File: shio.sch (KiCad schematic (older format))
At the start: 82 parts, among them J1 10118193-0001LF, U1 LM66100DCKT, U2 MAX38640AENT+, U3 NRF52840-CKAA-R7, U4 LM66100DCKT, U5 BMA400, U6 W25N01GVZEIG_TR, U8 SiP32431DR3, Y1 32.768kHz, Y3 32MHz

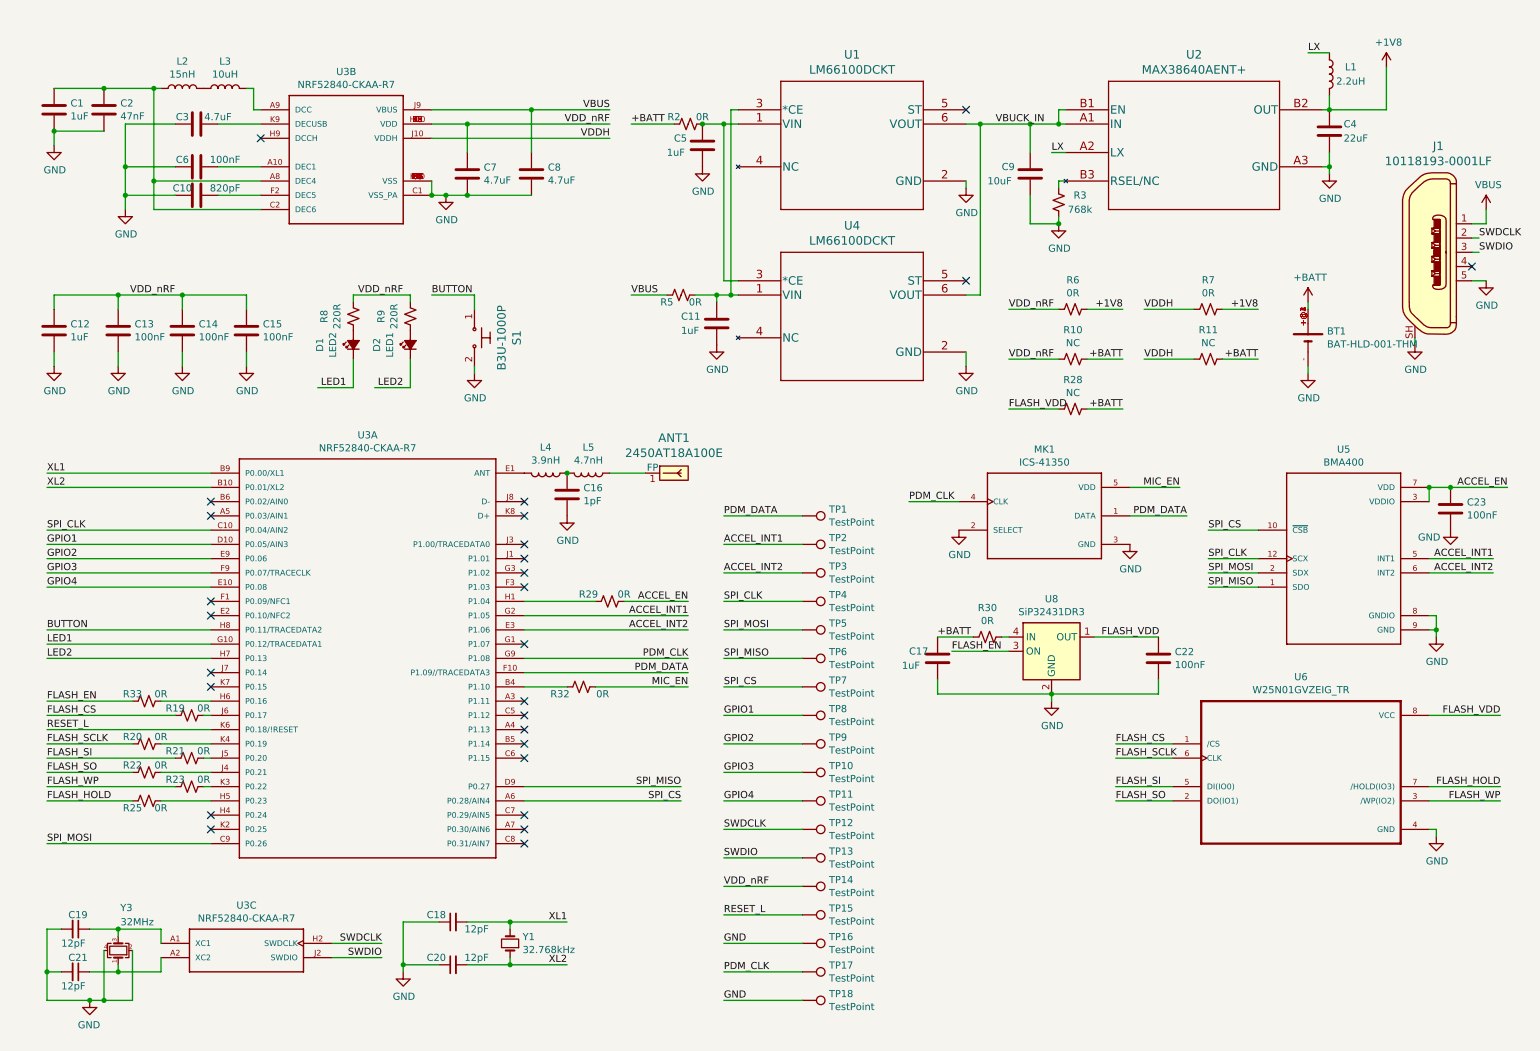
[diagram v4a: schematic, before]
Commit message: Cleaned up schematic, modified sheet
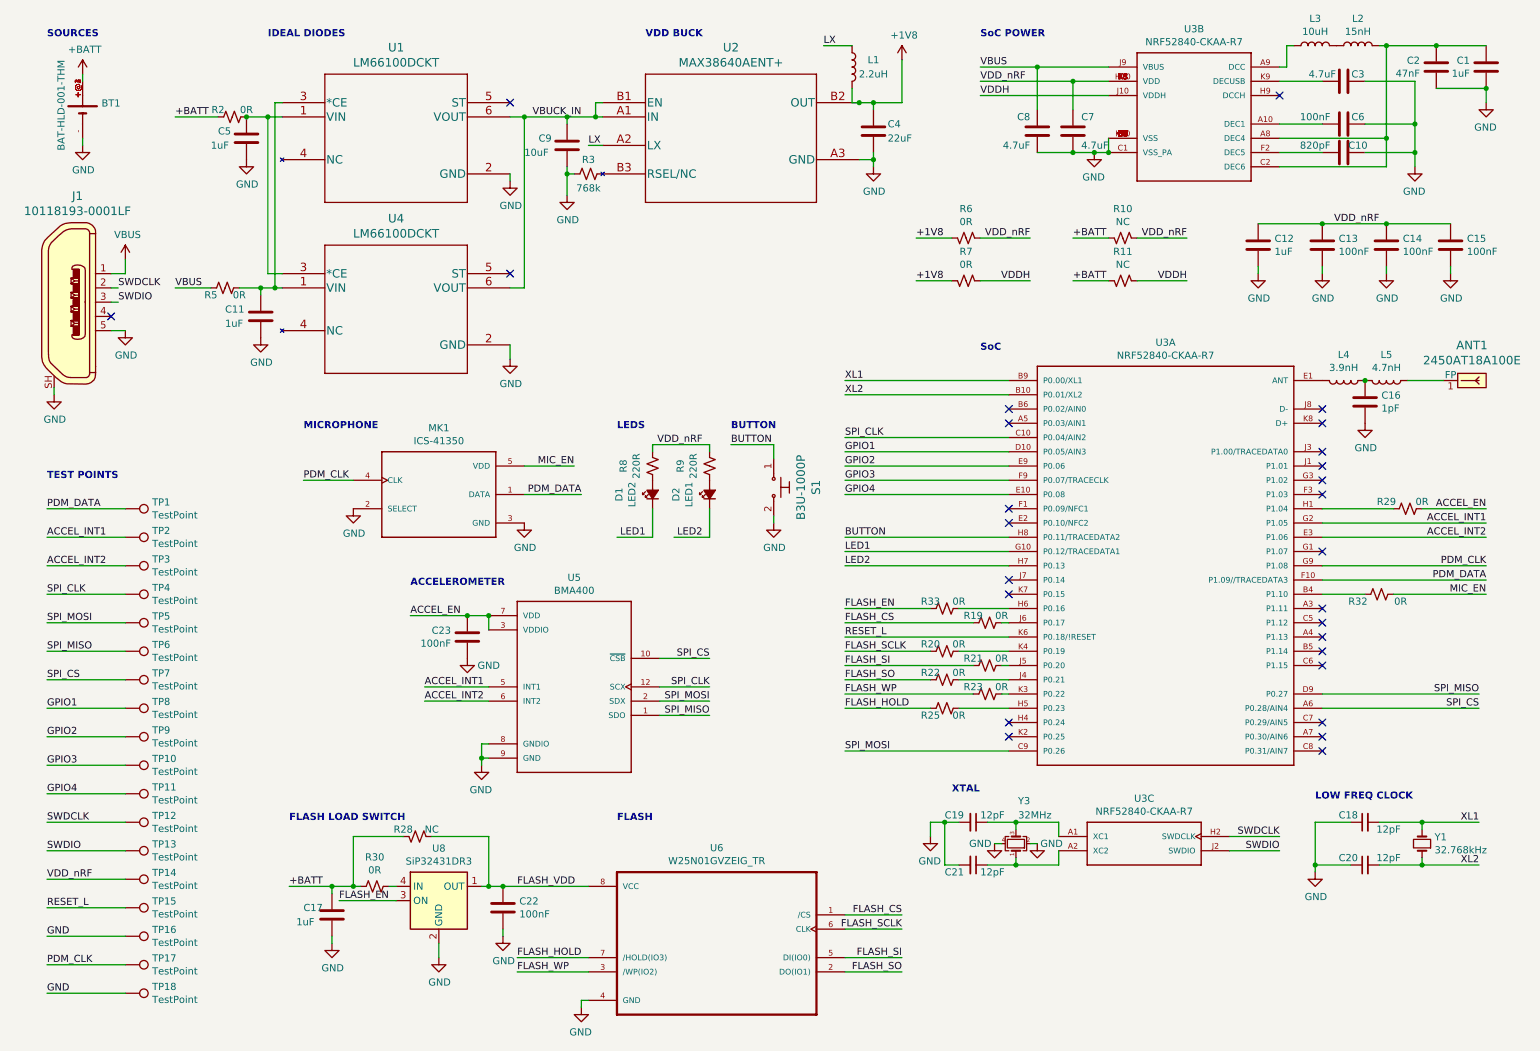
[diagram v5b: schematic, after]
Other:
- note added: "ACCELEROMETER"
- note added: "BUTTON"
- note added: "FLASH"
- note added: "FLASH LOAD SWITCH"
- note added: "IDEAL DIODES"
- note added: "LEDS"
- note added: "LOW FREQ CLOCK"
- note added: "MICROPHONE"
- note added: "SOURCES"
- note added: "SoC"
- note added: "SoC POWER"
- note added: "TEST POINTS\n"
- note added: "VDD BUCK"
- note added: "XTAL"
- moved on the sheet: ANT1, BT1, C1, C10, C11, C12, C13, C14, C15, C16, C17, C18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

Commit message: More routing
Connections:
- net ACCEL_INT1: now also U3.K2 (P0.25); no longer U3.G2 (P1.05)
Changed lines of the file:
@@
 Text Label 10900 4200 2    50   ~ 0
 ACCEL_INT2
-Text Label 10900 4100 2    50   ~ 0
+Text Label 6400 5600 0    50   ~ 0
 ACCEL_INT1
 Text Label 10900 4400 2    50   ~ 0
@@
 NoConn ~ 9750 5600
 NoConn ~ 9750 5500
-NoConn ~ 7550 5600
 NoConn ~ 7550 5500
 NoConn ~ 7550 4600
@@
 	7600 6200 7900 6200
 Wire Wire Line
-	9750 4100 10900 4100
-Wire Wire Line
 	9750 4200 10900 4200
 Wire Wire Line
@@
 Text Notes 800  700  0    50   ~ 10
 SOURCES
+Wire Wire Line
+	6400 5600 7550 5600
+NoConn ~ 9750 4100
 $EndSCHEMATC

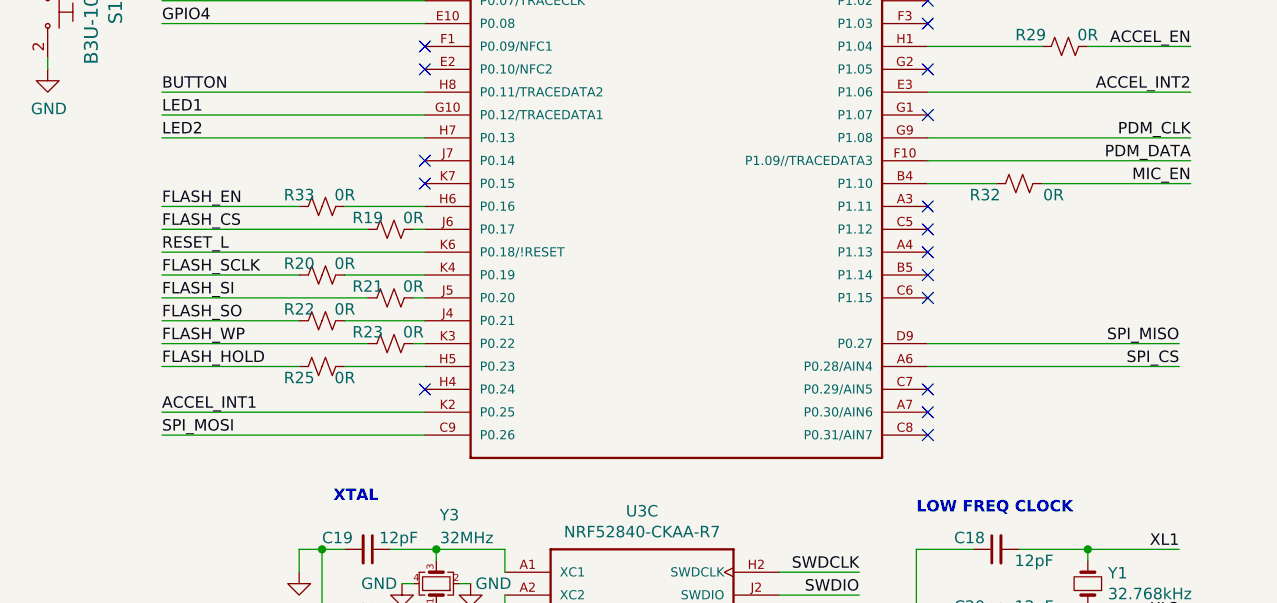
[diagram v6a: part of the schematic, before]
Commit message: First pass at routing done
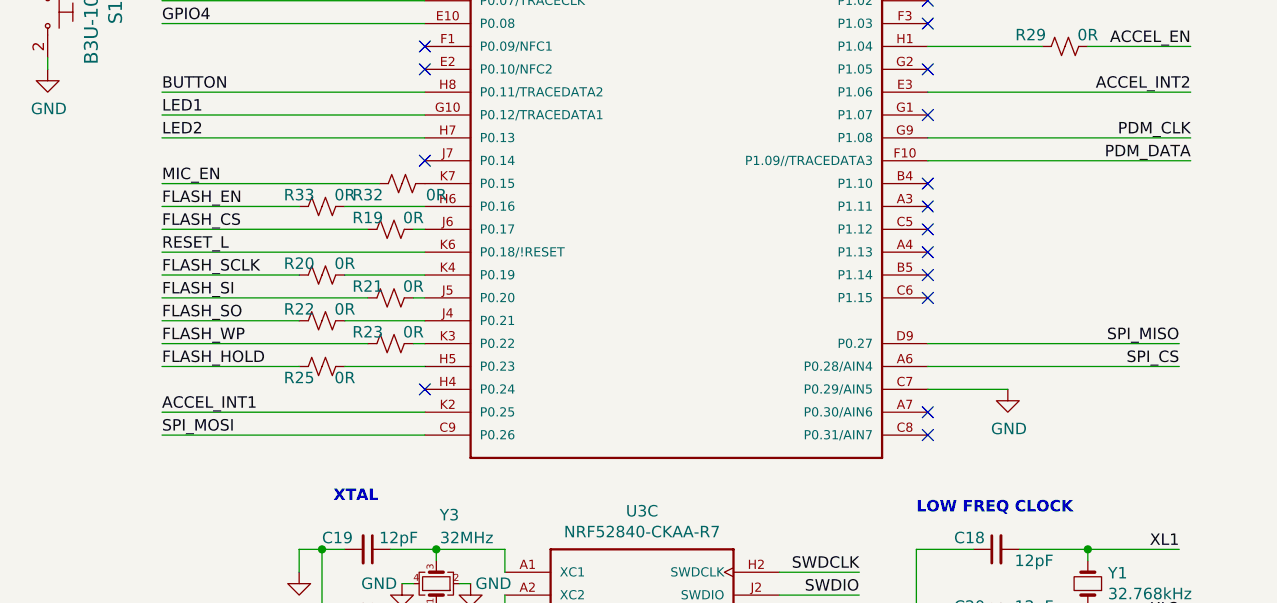
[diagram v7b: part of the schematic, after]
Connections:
- net GND: now also U3.C7 (P0.29/AIN5)
- net MIC_EN: now also R32.2; no longer R32.1
- net at U3.B4 (P1.10): no longer R32.2
- net at U3.K7 (P0.15): now also R32.1
- no-connect marks 27 -> 26
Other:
- moved on the sheet: R32
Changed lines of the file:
@@
 NoConn ~ 9750 5700
 NoConn ~ 9750 5600
-NoConn ~ 9750 5500
 NoConn ~ 7550 5500
-NoConn ~ 7550 4600
 NoConn ~ 7550 4500
 NoConn ~ 7550 4100
@@
 	0    -1   1    0
 $EndComp
-Text Label 10900 4600 2    50   ~ 0
+Text Label 6400 4600 0    50   ~ 0
 MIC_EN
-Wire Wire Line
-	10250 4600 10900 4600
-Wire Wire Line
-	10050 4600 9750 4600
 Text Label 10900 4000 2    50   ~ 0
 ACCEL_EN
@@
 L Device:R_Small_US R32
 U 1 1 5FAB45C8
-P 10150 4600
-F 0 "R32" V 10200 4450 50  0000 C CNN
-F 1 "0R" V 10200 4750 50  0000 C CNN
-F 2 "Resistor_SMD:R_0201_0603Metric" H 10150 4600 50  0001 C CNN
-F 3 "~" H 10150 4600 50  0001 C CNN
-	1    10150 4600
+P 7450 4600
+F 0 "R32" V 7500 4450 50  0000 C CNN
+F 1 "0R" V 7500 4750 50  0000 C CNN
+F 2 "Resistor_SMD:R_0201_0603Metric" H 7450 4600 50  0001 C CNN
+F 3 "~" H 7450 4600 50  0001 C CNN
+	1    7450 4600
 	0    1    1    0
 $EndComp
@@
 Wire Wire Line
 	6400 3600 7550 3600
-$Comp
-L NRF52840-CKAA-R7:NRF52840-CKAA-R7 U3
-U 1 1 5EF48FF1
-P 8650 4400
-F 0 "U3" H 8650 5967 50  0000 C CNN
-F 1 "NRF52840-CKAA-R7" H 8650 5876 50  0000 C CNN
-F 2 "Shio:BGA94N35P10X10_360X354X51N" H 8650 4400 50  0001 L BNN
-F 3 "1.1" H 8650 4400 50  0001 L BNN
-F 4 "Nordic" H 8650 4400 50  0001 L BNN "Field4"
-F 5 "0.514mm" H 8650 4400 50  0001 L BNN "Field5"
-F 6 "IPC7351B" H 8650 4400 50  0001 L BNN "Field6"
-	1    8650 4400
-	1    0    0    -1
-$EndComp
 NoConn ~ 7550 3300
 NoConn ~ 7550 3400
@@
 	6400 5600 7550 5600
 NoConn ~ 9750 4100
+Wire Wire Line
+	7350 4600 6400 4600
+NoConn ~ 9750 4600
+$Comp
+L power:GND #PWR?
+U 1 1 5F2067A7
+P 10100 5500
+F 0 "#PWR?" H 10100 5250 50  0001 C CNN
+F 1 "GND" H 10105 5327 50  0000 C CNN
+F 2 "" H 10100 5500 50  0001 C CNN
+F 3 "" H 10100 5500 50  0001 C CNN
+	1    10100 5500
+	1    0    0    -1
+$EndComp
+$Comp
+L NRF52840-CKAA-R7:NRF52840-CKAA-R7 U3
+U 1 1 5EF48FF1
+P 8650 4400
+F 0 "U3" H 8650 5967 50  0000 C CNN
+F 1 "NRF52840-CKAA-R7" H 8650 5876 50  0000 C CNN
+F 2 "Shio:BGA94N35P10X10_360X354X51N" H 8650 4400 50  0001 L BNN
+F 3 "1.1" H 8650 4400 50  0001 L BNN
+F 4 "Nordic" H 8650 4400 50  0001 L BNN "Field4"
+F 5 "0.514mm" H 8650 4400 50  0001 L BNN "Field5"
+F 6 "IPC7351B" H 8650 4400 50  0001 L BNN "Field6"
+	1    8650 4400
+	1    0    0    -1
+$EndComp
+Wire Wire Line
+	9750 5500 10100 5500
 $EndSCHEMATC

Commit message: Move ACCEL_INT1 to pin 1.7 as 0.25 didn't work on the dev kit
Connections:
- net ACCEL_INT1: now also U3.G1 (P1.07); no longer U3.K2 (P0.25)
- no-connect marks 26 -> 25
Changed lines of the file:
@@
 Text Label 10900 4200 2    50   ~ 0
 ACCEL_INT2
-Text Label 6400 5600 0    50   ~ 0
-ACCEL_INT1
 Text Label 10900 4400 2    50   ~ 0
 PDM_CLK
@@
 NoConn ~ 9750 4800
 NoConn ~ 9750 4700
-NoConn ~ 9750 4300
 NoConn ~ 9750 3900
 NoConn ~ 9750 3800
@@
 Text Notes 800  700  0    50   ~ 10
 SOURCES
-Wire Wire Line
-	6400 5600 7550 5600
 NoConn ~ 9750 4100
 Wire Wire Line
@@
 Wire Wire Line
 	9750 5500 10100 5500
+Text Label 10900 4300 2    50   ~ 0
+ACCEL_INT1
+Wire Wire Line
+	9750 4300 10900 4300
 $EndSCHEMATC
